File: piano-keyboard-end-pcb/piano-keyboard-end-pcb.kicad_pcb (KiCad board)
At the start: 2 copper layers, 25.4 x 61 mm, 12 parts, among them J1 Conn_01x03_Male, J2 Conn_01x01_Male, J3 Conn_01x02_Male, J4 Conn_01x02_Male, J5 Conn_01x05_Female, U1 74165

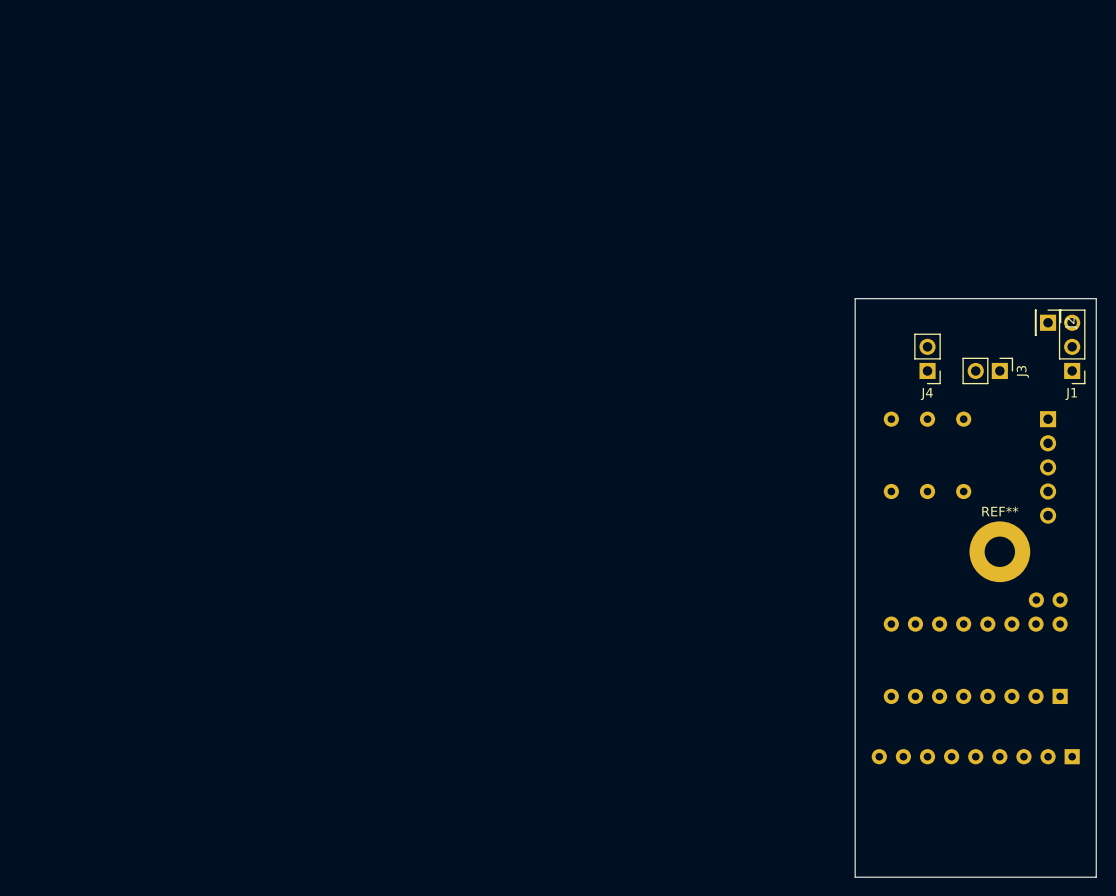
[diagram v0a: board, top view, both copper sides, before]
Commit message: finish adding footprints, including custom one for 1/4" mono jack; do rough part layout
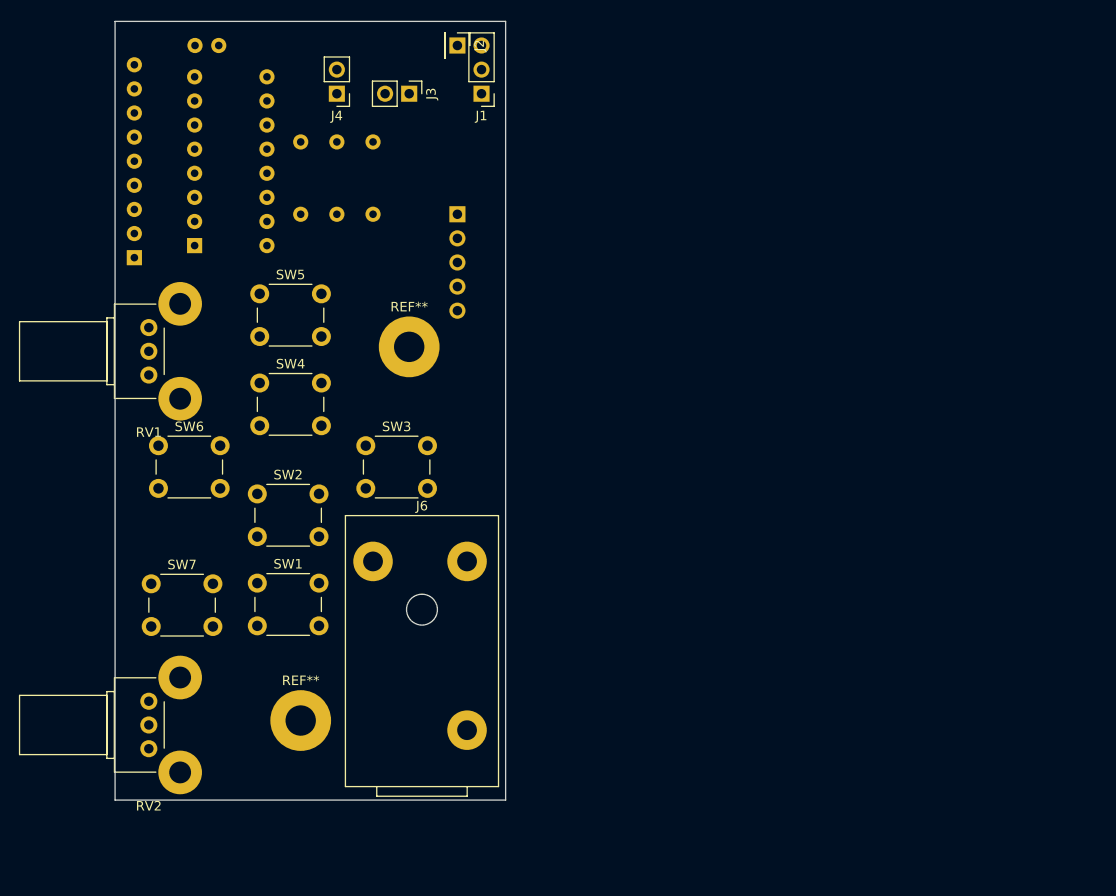
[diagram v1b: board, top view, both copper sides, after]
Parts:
- added J6: AudioJack2, piano-keyboard-end-pcb:Switchcraft_RA49B11, F.Cu at (106.8, 98.8)
- added REF**: MountingHole_3.2mm_M3_Pad, MountingHole:MountingHole_3.2mm_M3_Pad, F.Cu at (94.0, 110.5)
- added RV1: R_POT_US, Potentiometer_THT:Potentiometer_Bourns_PTV09A-2_Single_Horizontal, F.Cu at (78.0, 69.1)
- added RV2: R_POT_US, Potentiometer_THT:Potentiometer_Bourns_PTV09A-2_Single_Horizontal, F.Cu at (78.0, 108.5)
- added SW1: SW_Push, Button_Switch_THT:SW_PUSH_6mm, F.Cu at (89.4, 96.0)
- added SW2: SW_Push, Button_Switch_THT:SW_PUSH_6mm, F.Cu at (89.4, 86.6)
- added SW3: SW_Push, Button_Switch_THT:SW_PUSH_6mm, F.Cu at (100.8, 81.5)
- added SW4: SW_Push, Button_Switch_THT:SW_PUSH_6mm, F.Cu at (89.7, 74.9)
- added SW5: SW_Push, Button_Switch_THT:SW_PUSH_6mm, F.Cu at (89.7, 65.5)
- added SW6: SW_Push, Button_Switch_THT:SW_PUSH_6mm, F.Cu at (79.0, 81.5)
- added SW7: SW_Push, Button_Switch_THT:SW_PUSH_6mm, F.Cu at (78.2, 96.1)
- moved RN1 111.9 mm to (76.5, 61.7), turned to 90 degrees
- moved C1 106.2 mm to (85.3, 39.4)
- moved U1 102.8 mm to (82.8, 60.5), turned to 0 degrees
- moved R3 68.7 mm to (101.6, 57.1)
- moved J2 68.7 mm to (110.5, 39.4)
- moved J4 68.7 mm to (97.8, 44.5)
- moved R1 68.7 mm to (94.0, 57.1)
- moved R2 68.7 mm to (97.8, 49.5)
- moved J1 68.7 mm to (113.0, 44.5)
- moved J3 68.7 mm to (105.4, 44.5)
- moved J5 65.9 mm to (110.5, 57.1)
- moved REF** 65.9 mm to (105.4, 71.1)
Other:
- board size 25.4 x 61 mm -> 41.1 x 82 mm

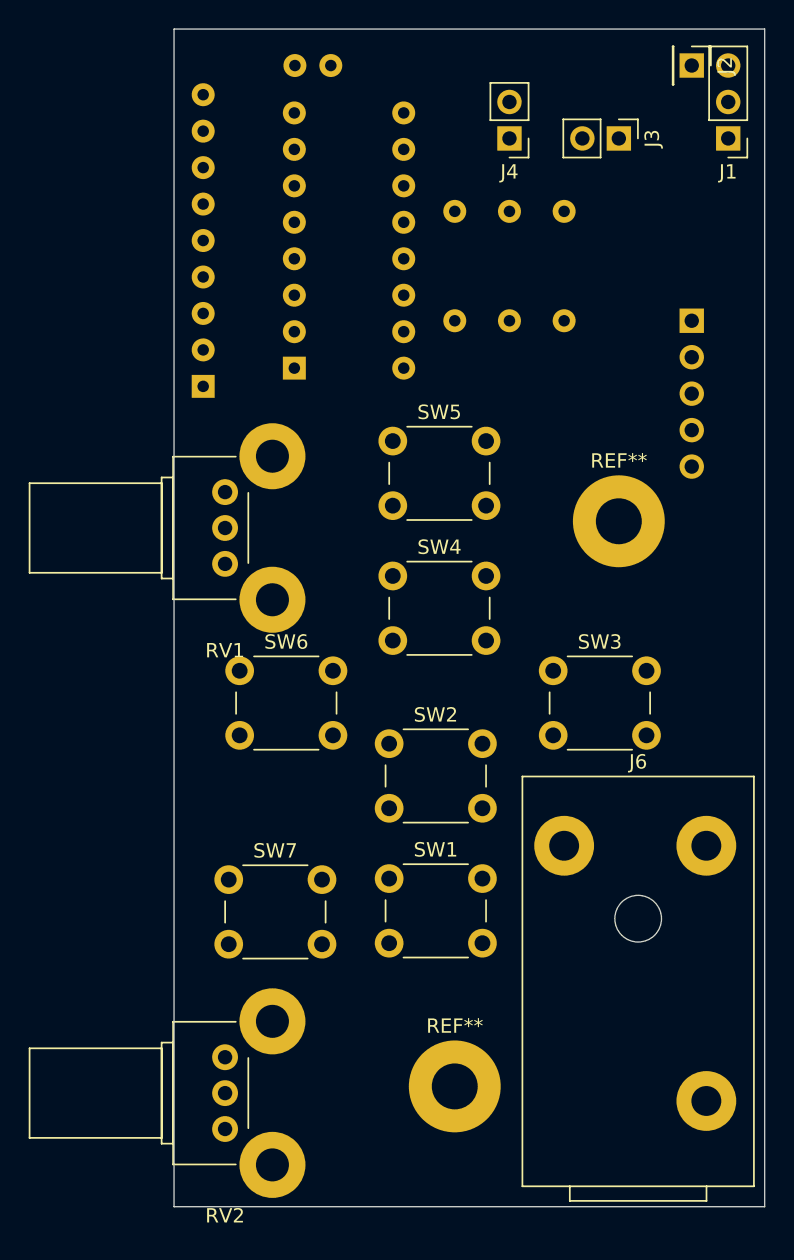
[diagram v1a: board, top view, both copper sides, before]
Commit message: put most parts on front side, align to 50mil grid
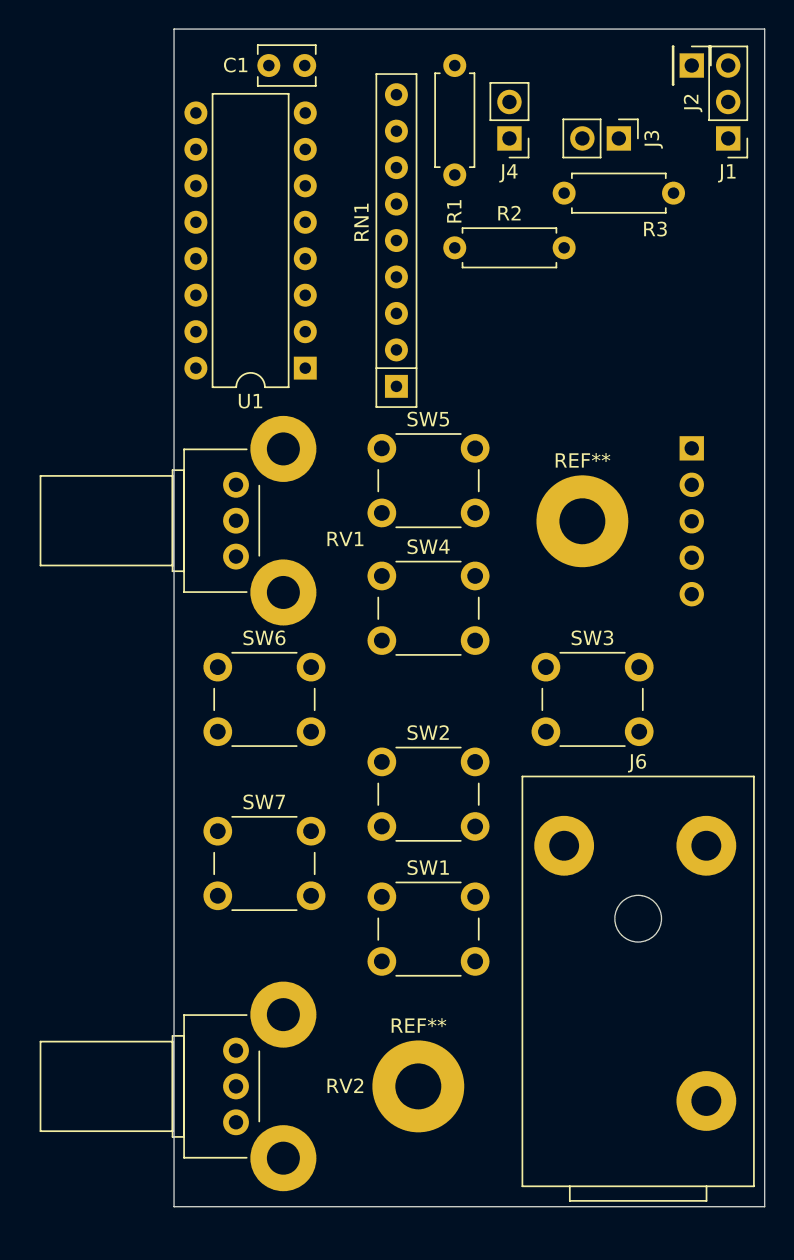
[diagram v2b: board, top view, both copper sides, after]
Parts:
- C1, R1, R2, R3, RN1, U1: moved to F.Cu
- moved R1 17.8 mm to (94.0, 39.4), turned to 270 degrees
- moved RN1 13.5 mm to (89.9, 61.7)
- moved J5 8.89 mm to (110.5, 66.0)
- moved R3 8.89 mm to (101.6, 48.3), turned to 0 degrees
- moved R2 4.58 mm to (94.0, 52.1), turned to 0 degrees
- moved C1 4.32 mm to (81.0, 39.4), turned to 0 degrees
- moved SW7 3.46 mm to (77.5, 92.7)
- moved REF** 2.54 mm to (91.4, 110.5)
- moved REF** 2.54 mm to (102.9, 71.1)
- moved SW6 1.55 mm to (77.5, 81.3)
- moved SW1 1.37 mm to (88.9, 97.3)
- moved SW2 1.37 mm to (88.9, 87.9)
- moved SW5 0.92 mm to (88.9, 66.0)
- moved RV1 0.92 mm to (78.7, 68.6)
- moved RV2 0.89 mm to (78.7, 108.0)
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
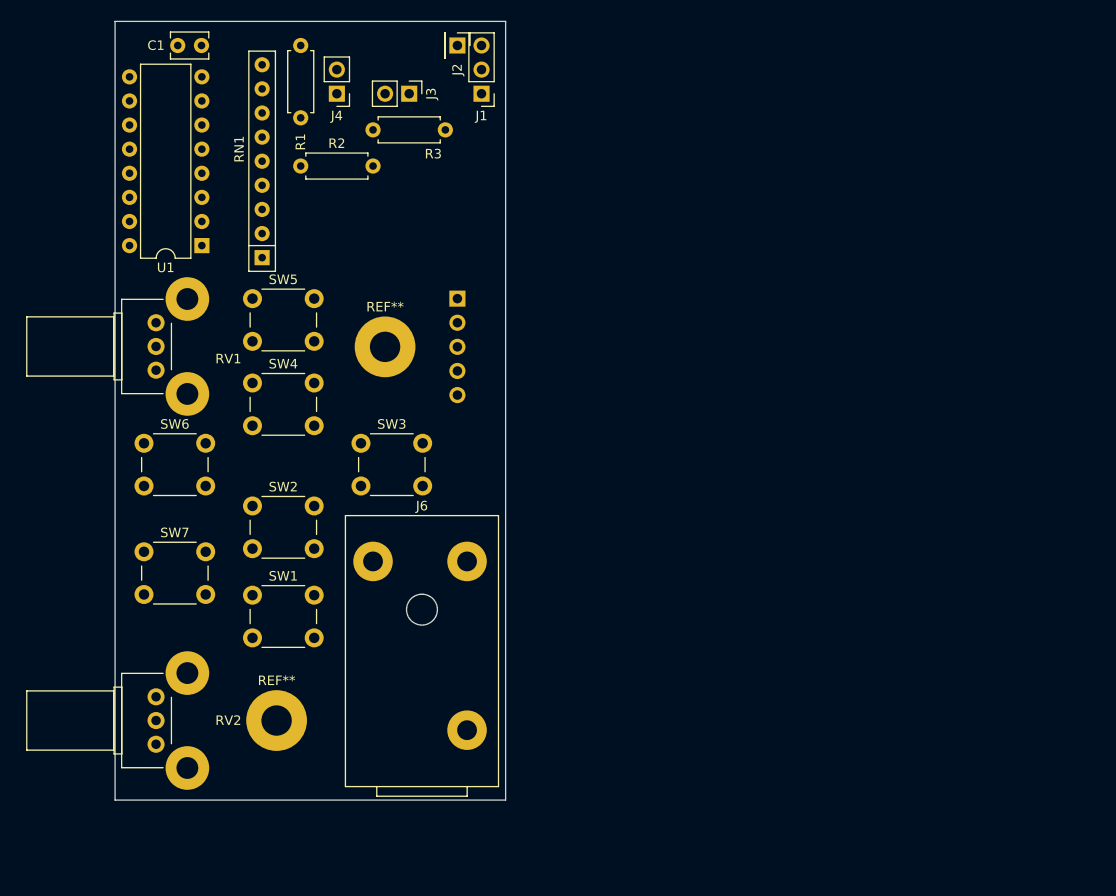
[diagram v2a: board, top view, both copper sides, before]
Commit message: add traces and silkscreen labels; rearrange buttons to make traces easier
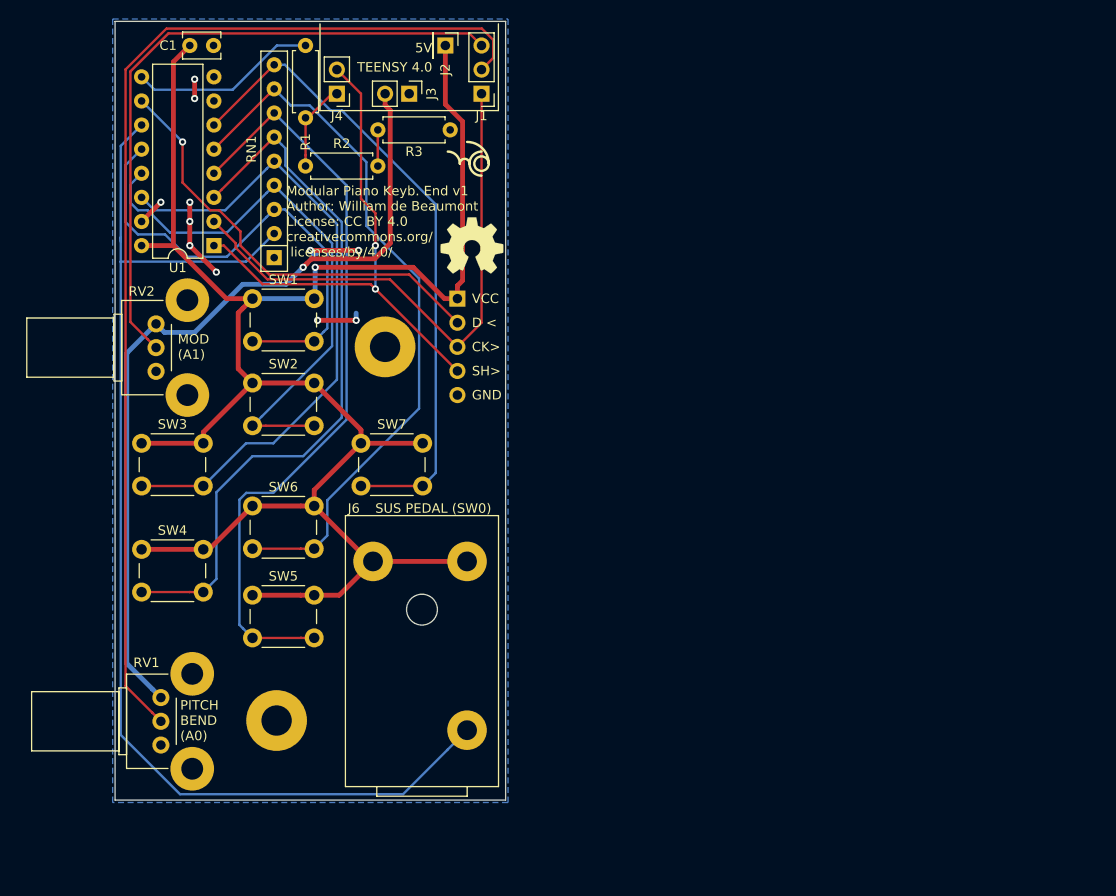
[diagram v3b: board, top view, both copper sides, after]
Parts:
- added REF**: OSHW-Symbol_6.7x6mm_SilkScreen, Symbol:OSHW-Symbol_6.7x6mm_SilkScreen, F.Cu at (112.0, 60.5)
- moved RV1 39.5 mm to (79.2, 108.1)
- moved RV2 39.3 mm to (78.7, 68.7)
- moved SW1 31.2 mm to (88.9, 66.0)
- moved SW5 31.2 mm to (88.9, 97.3)
- moved SW7 25.6 mm to (100.3, 81.3)
- moved SW3 23.1 mm to (77.2, 81.3)
- moved SW4 21.1 mm to (77.2, 92.5)
- moved SW6 13.2 mm to (88.9, 87.9)
- moved SW2 13.0 mm to (88.9, 74.9)
- moved C1 1.27 mm to (82.3, 39.4)
- moved RN1 1.27 mm to (91.2, 61.7)
- moved J2 1.27 mm to (109.2, 39.4)
- moved U1 1.27 mm to (84.8, 60.5)
- moved R3 0.51 mm to (102.1, 48.3)
- moved R1 0.51 mm to (94.5, 39.4)
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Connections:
- REF** pad 1: (no net) -> GND (x2)
- RV1 pad : (no net) -> GND
- RV2 pad : (no net) -> GND
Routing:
- net VCC: track 0.00 -> 197.6 mm, vias 0 -> 1
- net Net-(J6-PadS): track 0.00 -> 124.8 mm
- net /A0-PITCH: track 0.00 -> 114.9 mm
- net +3V3: track 0.00 -> 87.1 mm, vias 0 -> 1
- net Net-(RN1-Pad7): track 0.00 -> 80.9 mm
- net Net-(RN1-Pad8): track 0.00 -> 76.0 mm
- net Net-(RN1-Pad6): track 0.00 -> 75.5 mm
- net /A1-MOD: track 0.00 -> 69.4 mm
- net Net-(RN1-Pad9): track 0.00 -> 68.8 mm
- net Net-(RN1-Pad5): track 0.00 -> 67.6 mm
- net Net-(RN1-Pad4): track 0.00 -> 60.0 mm
- net /CLOCK: track 0.00 -> 59.1 mm
- net /MOSI-SHIFT: track 0.00 -> 55.9 mm, vias 0 -> 2
- net Net-(RN1-Pad3): track 0.00 -> 51.6 mm
- net /DATA_IN: track 0.00 -> 46.3 mm, vias 0 -> 1
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- added copper zone on B.Cu, net GND
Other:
- board text added: "5V"
- board text added: "CK>"
- board text added: "D <"
- board text added: "GND"
- board text added: "MOD (A1)"
- board text added: "Modular Piano Keyb. End v1 Author: William de Beaumont License: CC BY 4.0 creativecommons.org/ licenses/by/4.0/"
- board text added: "PITCH BEND (A0)"
- board text added: "SH>"
- board text added: "SUS PEDAL (SW0)"
- board text added: "TEENSY 4.0"
- board text added: "VCC"
